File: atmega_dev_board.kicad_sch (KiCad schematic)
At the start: 41 parts, among them J1 1x15 Pin Header, J2 USB_C_Receptacle_USB2.0_16P, J3 1x15 Pin Header, J4 2x3 Pin Header, SW1 Push Button, SW2 Push Button, U1 78L05G-AB3-R, U2 HT7533-1, U3 ATmega328P-A, U4 CP2102-GMR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

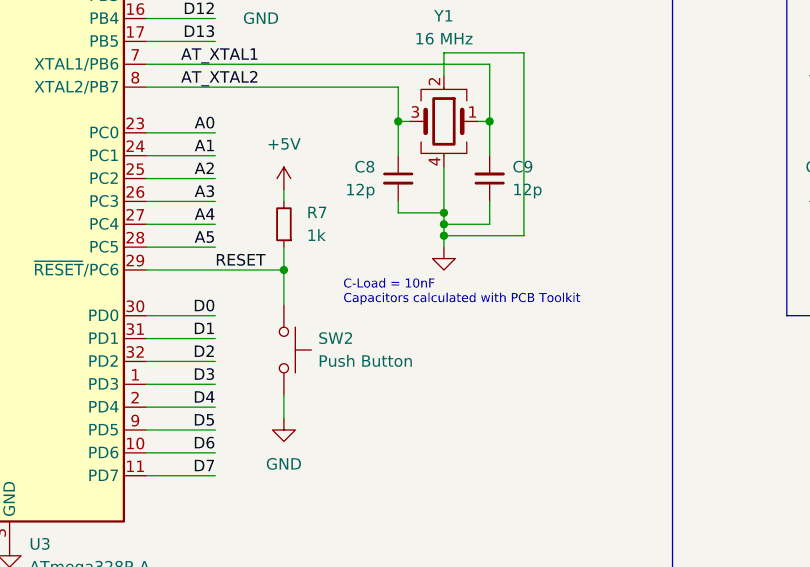
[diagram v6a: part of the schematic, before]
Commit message: Fix via sizing and other small changes
* Update part numbers
* Update BOM
* Slight fixes to schematic
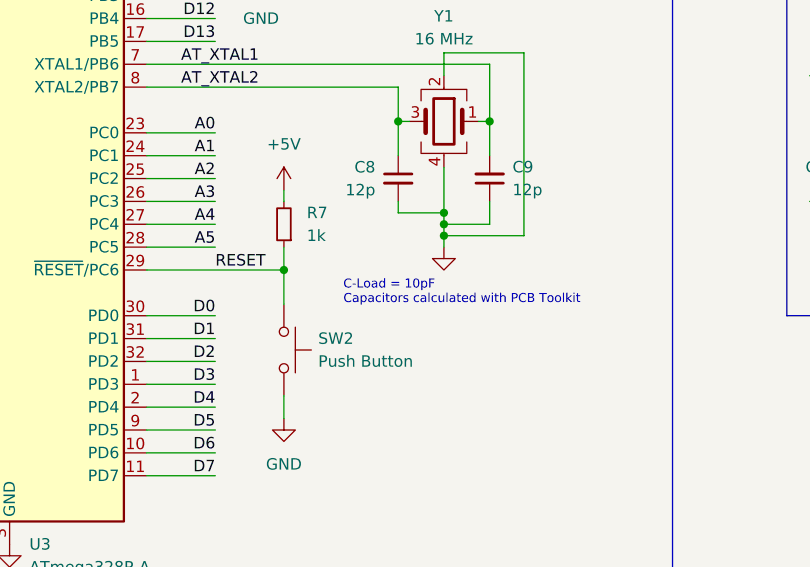
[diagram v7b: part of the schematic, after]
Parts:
- C1, C3: JLCPCB Part # (none) -> C19702; JLCPCB Part# C19702 -> (none)
- C10, C11, C12, C13, C15, C2, C4, C5, C6, C7: JLCPCB Part # (none) -> C14663; JLCPCB Part# C14663 -> (none)
- C8, C9: JLCPCB Part # (none) -> C38523; JLCPCB Part# C38523 -> (none)
- D1: JLCPCB Part # (none) -> C191023; JLCPCB Part# C191023 -> (none)
- D2, D4: JLCPCB Part # (none) -> C2286; JLCPCB Part# C2286 -> (none)
- D3: JLCPCB Part # (none) -> C2843785; JLCPCB Part# C2843785 -> (none)
- J2: JLCPCB Part # (none) -> C7527694; JLCPCB Part# C7527694 -> (none)
- R1, R2, R7, R8, R9: JLCPCB Part # (none) -> C21190; JLCPCB Part# C21190 -> (none)
- R3, R4: JLCPCB Part # (none) -> C23186; JLCPCB Part# C23186 -> (none)
- SW1, SW2: JLCPCB Part # (none) -> C318884; JLCPCB Part# C318884 -> (none)
- U1: JLCPCB Part # (none) -> C71136; JLCPCB Part# C71136 -> (none)
- U2: JLCPCB Part # (none) -> C14289; JLCPCB Part# C14289 -> (none)
- U3: JLCPCB Part # (none) -> C14877; JLCPCB Part# C14877 -> (none)
- U4: JLCPCB Part # (none) -> C6568; JLCPCB Part# C6568 -> (none)
- Y1: JLCPCB Part # (none) -> C13738; JLCPCB Part# C13738 -> (none)
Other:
- note added: "C-Load = 10pF Capacitors calculated with PCB Toolkit"
- note removed: "C-Load = 10nF Capacitors calculated with PCB Toolkit"
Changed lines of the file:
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@@
 	(title_block
 		(title "Arduino Dolly")
-		(date "2024-06-02")
-		(rev "Rev 0")
+		(date "2024-06-05")
+		(rev "Rev 1")
 	)
 	(junction
@@
 		)
 	)
-	(text "C-Load = 10nF\nCapacitors calculated with PCB Toolkit"
+	(text "C-Load = 10pF\nCapacitors calculated with PCB Toolkit"
 		(exclude_from_sim no)
 		(at 174.244 130.81 0)
@@
 			)
 		)
-		(property "JLCPCB Part#" "C23186"
+		(property "Manufacturer Part#" "0603WAF5101T5E"
 			(at 80.01 45.72 0)
 			(effects
@@
 			)
 		)
-		(property "Manufacturer Part#" "0603WAF5101T5E"
+		(property "JLCPCB Part #" "C23186"
 			(at 80.01 45.72 0)
 			(effects
@@
 			)
 		)
-		(property "JLCPCB Part#" "C2843785"
+		(property "Manufacturer Part#" "XL-5050RGBC-WS2812B"
 			(at 254 120.65 0)
 			(effects
@@
 			)
 		)
-		(property "Manufacturer Part#" "XL-5050RGBC-WS2812B"
+		(property "JLCPCB Part #" "C2843785"
 			(at 254 120.65 0)
 			(effects
@@
 			)
 		)
-		(property "JLCPCB Part#" "C38523"
+		(property "Manufacturer Part#" "CL10C120JB8NNNC"
 			(at 180.34 118.11 0)
 			(effects
@@
 			)
 		)
-		(property "Manufacturer Part#" "CL10C120JB8NNNC"
+		(property "JLCPCB Part #" "C38523"
 			(at 180.34 118.11 0)
 			(effects
@@
 			)
 		)
-		(property "JLCPCB Part#" "C6568"
+		(property "Manufacturer Part#" "CP2102-GMR"
 			(at 50.8 148.59 0)
 			(effects
@@
 			)
 		)
-		(property "Manufacturer Part#" "CP2102-GMR"
+		(property "JLCPCB Part #" "C6568"
 			(at 50.8 148.59 0)
 			(effects
@@
 			)
 		)
-		(property "JLCPCB Part#" "C14663"
+		(property "Manufacturer Part#" "CC0603KRX7R9BB104"
 			(at 71.12 133.35 0)
 			(effects
@@
 			)
 		)
-		(property "Manufacturer Part#" "CC0603KRX7R9BB104"
+		(property "JLCPCB Part #" "C14663"
 			(at 71.12 133.35 0)
 			(effects
@@
 			)
 		)
-		(property "JLCPCB Part#" "C21190"
+		(property "Manufacturer Part#" "0603WAF1001T5E"
 			(at 140.97 41.91 0)
 			(effects
@@
 			)
 		)
-		(property "Manufacturer Part#" "0603WAF1001T5E"
+		(property "JLCPCB Part #" "C21190"
 			(at 140.97 41.91 0)
 			(effects
@@
 			)
 		)
-		(property "JLCPCB Part#" "C14663"
+		(property "Manufacturer Part#" "CC0603KRX7R9BB104"
 			(at 27.94 113.03 0)
 			(effects
@@
 			)
 		)
-		(property "Manufacturer Part#" "CC0603KRX7R9BB104"
+		(property "JLCPCB Part #" "C14663"
 			(at 27.94 113.03 0)
 			(effects
@@
 			)
 		)
-		(property "JLCPCB Part#" "C38523"
+		(property "Manufacturer Part#" "CL10C120JB8NNNC"
 			(at 190.5 118.11 0)
 			(effects
@@
 			)
 		)
-		(property "Manufacturer Part#" "CL10C120JB8NNNC"
+		(property "JLCPCB Part #" "C38523"
 			(at 190.5 118.11 0)
 			(effects
@@
 			)
 		)
-		(property "JLCPCB Part#" "C14663"
+		(property "Manufacturer Part#" "CC0603KRX7R9BB104"
 			(at 129.54 44.45 0)
 			(effects
@@
 			)
 		)
-		(property "Manufacturer Part#" "CC0603KRX7R9BB104"
+		(property "JLCPCB Part #" "C14663"
 			(at 129.54 44.45 0)
 			(effects
@@
 			)
 		)
-		(property "JLCPCB Part#" "C23186"
+		(property "Manufacturer Part#" "0603WAF5101T5E"
 			(at 72.39 45.72 0)
 			(effects
@@
 			)
 		)
-		(property "Manufacturer Part#" "0603WAF5101T5E"
+		(property "JLCPCB Part #" "C23186"
 			(at 72.39 45.72 0)
 			(effects
@@
 			)
 		)
-		(property "JLCPCB Part#" "C14663"
+		(property "Manufacturer Part#" "CC0603KRX7R9BB104"
 			(at 115.57 77.47 0)
 			(effects
@@
 			)
 		)
-		(property "Manufacturer Part#" "CC0603KRX7R9BB104"
+		(property "JLCPCB Part #" "C14663"
 			(at 115.57 77.47 0)
 			(effects
@@
 			)
 		)
-		(property "JLCPCB Part#" "C14663"
+		(property "Manufacturer Part#" "CC0603KRX7R9BB104"
 			(at 27.94 151.13 0)
 			(effects
@@
 			)
 		)
-		(property "Manufacturer Part#" "CC0603KRX7R9BB104"
+		(property "JLCPCB Part #" "C14663"
 			(at 27.94 151.13 0)
 			(effects
@@
 			)
 		)
-		(property "JLCPCB Part#" "C21190"
+		(property "Manufacturer Part#" "0603WAF1001T5E"
 			(at 167.64 123.19 0)
 			(effects
@@
 			)
 		)
-		(property "Manufacturer Part#" "0603WAF1001T5E"
+		(property "JLCPCB Part #" "C21190"
 			(at 167.64 123.19 0)
 			(effects
@@
 			)
 		)
-		(property "JLCPCB Part#" "C14663"
+		(property "Manufacturer Part#" "CC0603KRX7R9BB104"
 			(at 52.07 80.01 0)
 			(effects
@@
 			)
 		)
-		(property "Manufacturer Part#" "CC0603KRX7R9BB104"
+		(property "JLCPCB Part #" "C14663"
 			(at 52.07 80.01 0)
 			(effects
@@
 			)
 		)
-		(property "JLCPCB Part#" "C2286"
+		(property "Manufacturer Part#" "KT-0603R"
 			(at 140.97 49.53 0)
 			(effects
@@
 			)
 		)
-		(property "Manufacturer Part#" "KT-0603R"
+		(property "JLCPCB Part #" "C2286"
 			(at 140.97 49.53 0)
 			(effects
@@
 			)
 		)
-		(property "JLCPCB Part#" "C191023"
+		(property "Manufacturer Part#" "1N5819WS"
 			(at 199.39 43.18 0)
 			(effects
@@
 			)
 		)
-		(property "Manufacturer Part#" "1N5819WS"
+		(property "JLCPCB Part #" "C191023"
 			(at 199.39 43.18 0)
 			(effects
@@
 			)
 		)
-		(property "JLCPCB Part#" "C14877"
+		(property "Manufacturer Part#" "ATMEGA328P-AU"
 			(at 137.16 120.65 0)
 			(effects
@@
 			)
 		)
-		(property "Manufacturer Part#" "ATMEGA328P-AU"
+		(property "JLCPCB Part #" "C14877"
 			(at 137.16 120.65 0)
 			(effects
@@
 			)
 		)
-		(property "JLCPCB Part#" "C19702"
+		(property "Manufacturer Part#" "CL10A106KP8NNNC"
 			(at 104.14 44.45 0)
 			(effects
@@
 			)
 		)
-		(property "Manufacturer Part#" "CL10A106KP8NNNC"
+		(property "JLCPCB Part #" "C19702"
 			(at 104.14 44.45 0)
 			(effects
@@
 			)
 		)
-		(property "JLCPCB Part#" "C7527694"
+		(property "Manufacturer Part#" "XUBF-0336-0817B"
 			(at 33.02 49.53 0)
 			(effects
@@
 			)
 		)
-		(property "Manufacturer Part#" "XUBF-0336-0817B"
+		(property "JLCPCB Part #" "C7527694"
 			(at 33.02 49.53 0)
 			(effects
@@
 			)
 		)
-		(property "JLCPCB Part#" "C21190"
+		(property "Manufacturer Part#" "0603WAF1001T5E"
 			(at 36.83 113.03 0)
 			(effects
@@
 			)
 		)
-		(property "Manufacturer Part#" "0603WAF1001T5E"
+		(property "JLCPCB Part #" "C21190"
 			(at 36.83 113.03 0)
 			(effects
@@
 			)
 		)
-		(property "JLCPCB Part#" "C13738"
+		(property "Manufacturer Part#" "X322516MLB4SI"
 			(at 185.42 111.76 0)
 			(effects
@@
 			)
 		)
-		(property "Manufacturer Part#" "X322516MLB4SI"
+		(property "JLCPCB Part #" "C13738"
 			(at 185.42 111.76 0)
 			(effects
@@
 			)
 		)
-		(property "JLCPCB Part#" "C14663"
+		(property "Manufacturer Part#" "CC0603KRX7R9BB104"
 			(at 124.46 77.47 0)
 			(effects
@@
 			)
 		)
-		(property "Manufacturer Part#" "CC0603KRX7R9BB104"
+		(property "JLCPCB Part #" "C14663"
 			(at 124.46 77.47 0)
 			(effects
@@
 			)
 		)
-		(property "JLCPCB Part#" "C21190"
+		(property "Manufacturer Part#" "0603WAF1001T5E"
 			(at 243.84 106.68 0)
 			(effects
@@
 			)
 		)
-		(property "Manufacturer Part#" "0603WAF1001T5E"
+		(property "JLCPCB Part #" "C21190"
 			(at 243.84 106.68 0)
 			(effects
@@
 			)
 		)
-		(property "JLCPCB Part#" "C19702"
+		(property "Manufacturer Part#" "CL10A106KP8NNNC"
 			(at 153.67 44.45 0)
 			(effects
@@
 			)
 		)
-		(property "Manufacturer Part#" "CL10A106KP8NNNC"
+		(property "JLCPCB Part #" "C19702"
 			(at 153.67 44.45 0)
 			(effects
@@
 			)
 		)
-		(property "JLCPCB Part#" "C318884"
+		(property "Manufacturer Part#" "TS-1187A-B-A-B"
 			(at 167.64 137.16 0)
 			(effects
@@
 			)
 		)
-		(property "Manufacturer Part#" "TS-1187A-B-A-B"
+		(property "JLCPCB Part #" "C318884"
 			(at 167.64 137.16 0)
 			(effects
@@
 			)
 		)
-		(property "JLCPCB Part#" "C14663"
+		(property "Manufacturer Part#" "CC0603KRX7R9BB104"
 			(at 179.07 44.45 0)
 			(effects
@@
 			)
 		)
-		(property "Manufacturer Part#" "CC0603KRX7R9BB104"
+		(property "JLCPCB Part #" "C14663"
 			(at 179.07 44.45 0)
 			(effects
@@
 			)
 		)
-		(property "JLCPCB Part#" "C14663"
+		(property "Manufacturer Part#" "CC0603KRX7R9BB104"
 			(at 106.68 77.47 0)
 			(effects
@@
 			)
 		)
-		(property "Manufacturer Part#" "CC0603KRX7R9BB104"
+		(property "JLCPCB Part #" "C14663"
 			(at 106.68 77.47 0)
 			(effects
@@
 			)
 		)
-		(property "JLCPCB Part#" "C2286"
+		(property "Manufacturer Part#" "KT-0603R"
 			(at 165.1 92.71 0)
 			(effects
@@
 			)
 		)
-		(property "Manufacturer Part#" "KT-0603R"
+		(property "JLCPCB Part #" "C2286"
 			(at 165.1 92.71 0)
 			(effects
@@
 			)
 		)
-		(property "JLCPCB Part#" "C21190"
+		(property "Manufacturer Part#" "0603WAF1001T5E"
 			(at 165.1 85.09 0)
 			(effects
@@
 			)
 		)
-		(property "Manufacturer Part#" "0603WAF1001T5E"
+		(property "JLCPCB Part #" "C21190"
 			(at 165.1 85.09 0)
 			(effects
@@
 			)
 		)
-		(property "JLCPCB Part#" "C14289"
+		(property "Manufacturer Part#" "HT7533-1"
 			(at 166.37 38.1 0)
 			(effects
@@
 			)
 		)
-		(property "Manufacturer Part#" "HT7533-1"
+		(property "JLCPCB Part #" "C14289"
 			(at 166.37 38.1 0)
 			(effects
@@
 			)
 		)
-		(property "JLCPCB Part#" "C14663"
+		(property "Manufacturer Part#" "CC0603KRX7R9BB104"
 			(at 106.68 95.25 0)
 			(effects
@@
 			)
 		)
-		(property "Manufacturer Part#" "CC0603KRX7R9BB104"
+		(property "JLCPCB Part #" "C14663"
 			(at 106.68 95.25 0)
 			(effects
@@
 			)
 		)
-		(property "JLCPCB Part#" "C318884"
+		(property "Manufacturer Part#" "TS-1187A-B-A-B"
 			(at 234.95 106.68 0)
 			(effects
@@
 			)
 		)
-		(property "Manufacturer Part#" "TS-1187A-B-A-B"
+		(property "JLCPCB Part #" "C318884"
 			(at 234.95 106.68 0)
 			(effects
@@
 			)
 		)
-		(property "JLCPCB Part#" "C71136"
+		(property "Manufacturer Part#" "78L05G-AB3-R"
 			(at 116.84 38.1 0)
 			(effects
@@
 			)
 		)
-		(property "Manufacturer Part#" "78L05G-AB3-R"
+		(property "JLCPCB Part #" "C71136"
 			(at 116.84 38.1 0)
 			(effects

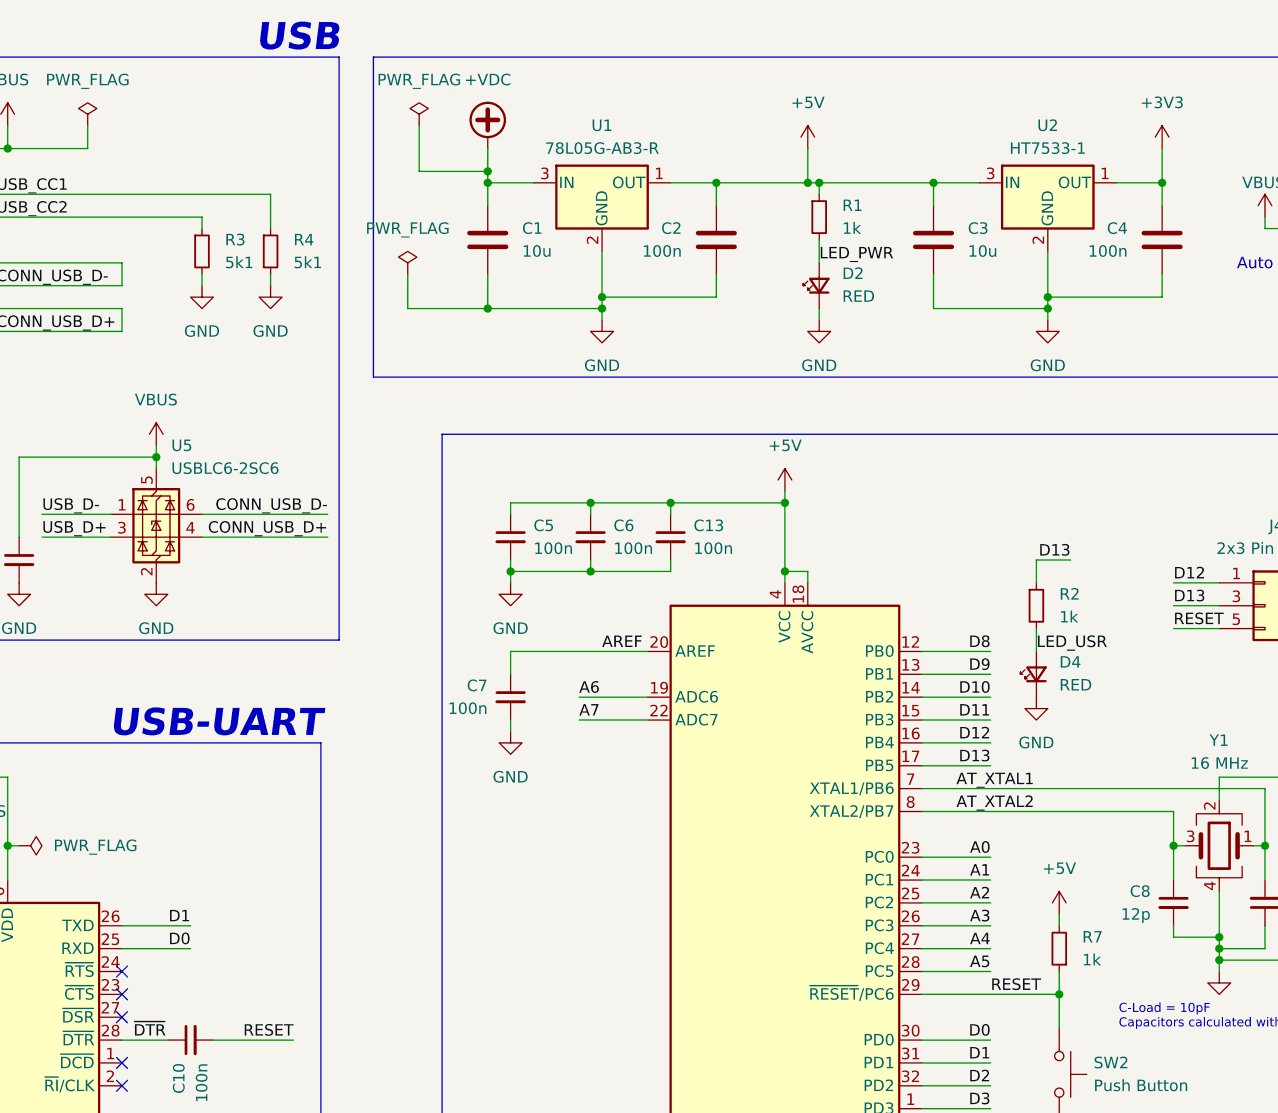
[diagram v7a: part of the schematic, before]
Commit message: fix: Fix UART mis-match. Fix VREG footprint
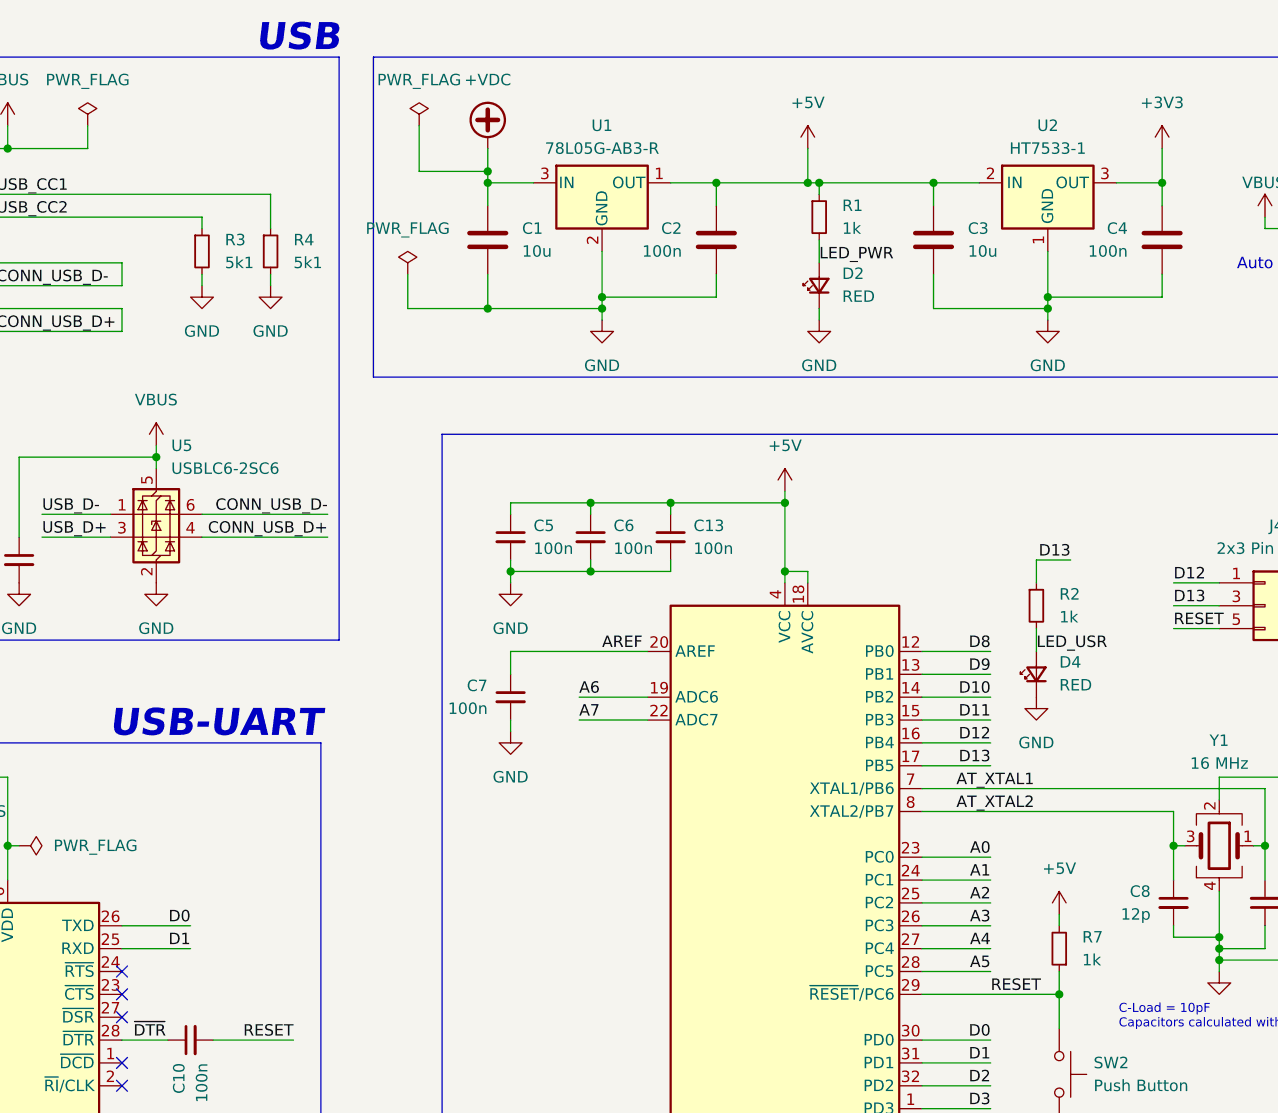
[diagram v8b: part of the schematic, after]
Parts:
- U2: symbol Regulator_Linear:L78L33_SOT89 -> dev_board:HT7533-1
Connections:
- net +3V3: now also U2.3 (OUT); no longer U2.1 (OUT)
- net +5V: now also U2.2 (IN); no longer U2.3 (IN)
- net D0: now also U4.26 (TXD); no longer U4.25 (RXD)
- net D1: now also U4.25 (RXD); no longer U4.26 (TXD)
- net GND: now also U2.1 (GND); no longer U2.2 (GND)
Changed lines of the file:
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@@
 	)
 	(label "D1"
-		(at 71.12 120.65 180)
+		(at 71.12 123.19 180)
 		(fields_autoplaced yes)
 		(effects
@@
 	)
 	(label "D0"
-		(at 71.12 123.19 180)
+		(at 71.12 120.65 180)
 		(fields_autoplaced yes)
 		(effects
@@
 	)
 	(symbol
-		(lib_id "Regulator_Linear:L78L33_SOT89")
-		(at 166.37 38.1 0)
+		(lib_id "dev_board:HT7533-1")
+		(at 166.37 39.37 0)
 		(unit 1)
 		(exclude_from_sim no)
@@
 		)
 		(property "Footprint" "Package_TO_SOT_SMD:SOT-89-3"
-			(at 166.37 33.02 0)
+			(at 166.37 34.29 0)
 			(effects
 				(font
@@
 		)
 		(property "Datasheet" "https://wmsc.lcsc.com/wmsc/upload/file/pdf/v2/lcsc/2312191111_Holtek-Semicon-HT7533-1_C14289.pdf"
-			(at 166.37 39.37 0)
+			(at 166.37 40.64 0)
 			(effects
 				(font
@@
 		)
 		(property "Description" "Positive 100mA 30V Linear Regulator, Fixed Output 3.3V, SOT-89"
-			(at 166.37 38.1 0)
+			(at 166.37 39.37 0)
 			(effects
 				(font
@@
 		)
 		(property "Sim.Device" ""
-			(at 166.37 38.1 0)
+			(at 166.37 39.37 0)
 			(effects
 				(font
@@
 		)
 		(property "Sim.Pins" ""
-			(at 166.37 38.1 0)
+			(at 166.37 39.37 0)
 			(effects
 				(font
@@
 		)
 		(property "Manufacturer Part#" "HT7533-1"
-			(at 166.37 38.1 0)
+			(at 166.37 39.37 0)
 			(effects
 				(font
@@
 		)
 		(property "JLCPCB Part #" "C14289"
-			(at 166.37 38.1 0)
+			(at 166.37 39.37 0)
 			(effects
 				(font
